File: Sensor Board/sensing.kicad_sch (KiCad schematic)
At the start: 12 parts, among them J4 CAN Bus Connector, U2 INA180, U5 INA180

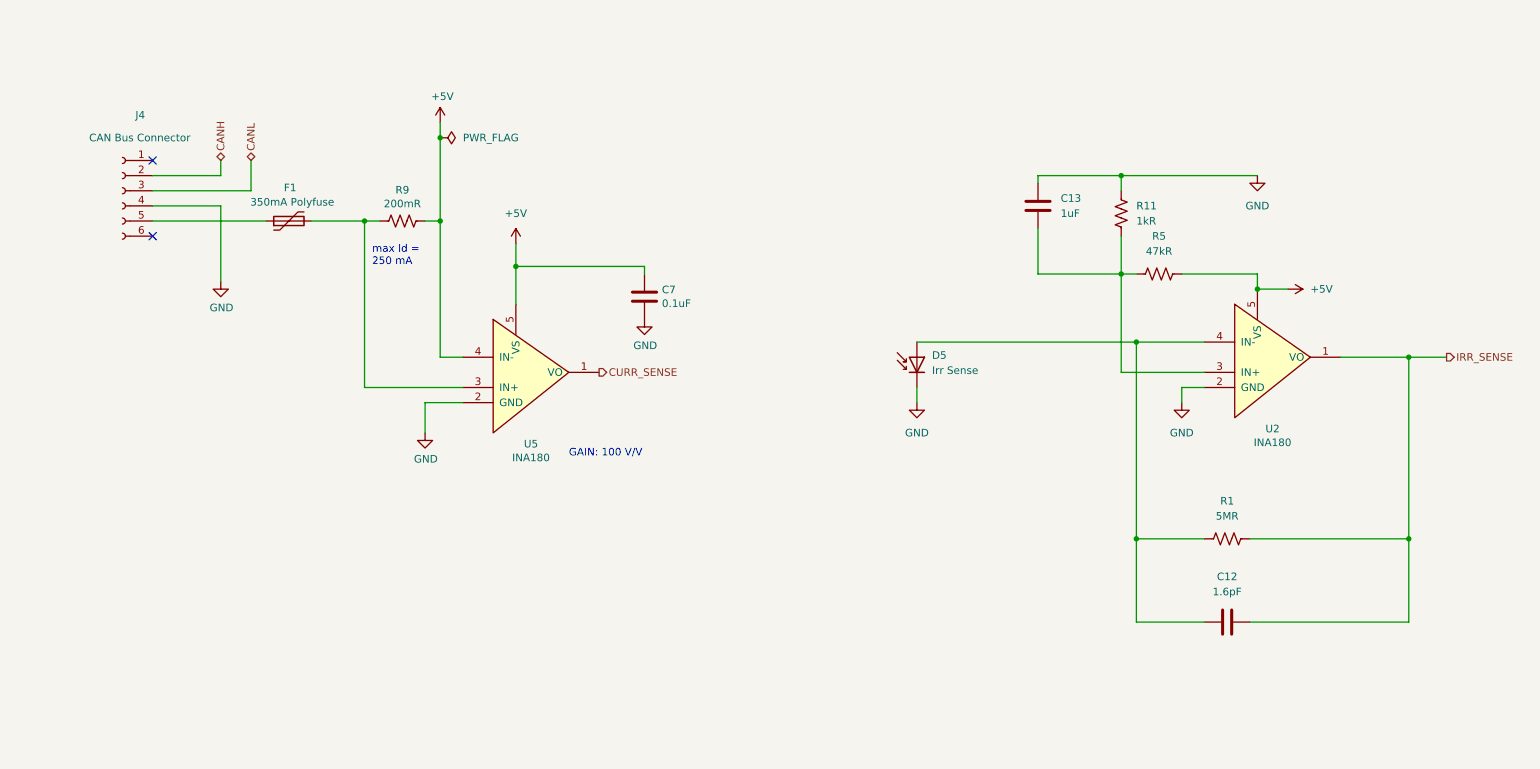
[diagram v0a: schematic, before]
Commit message: Switch op amp
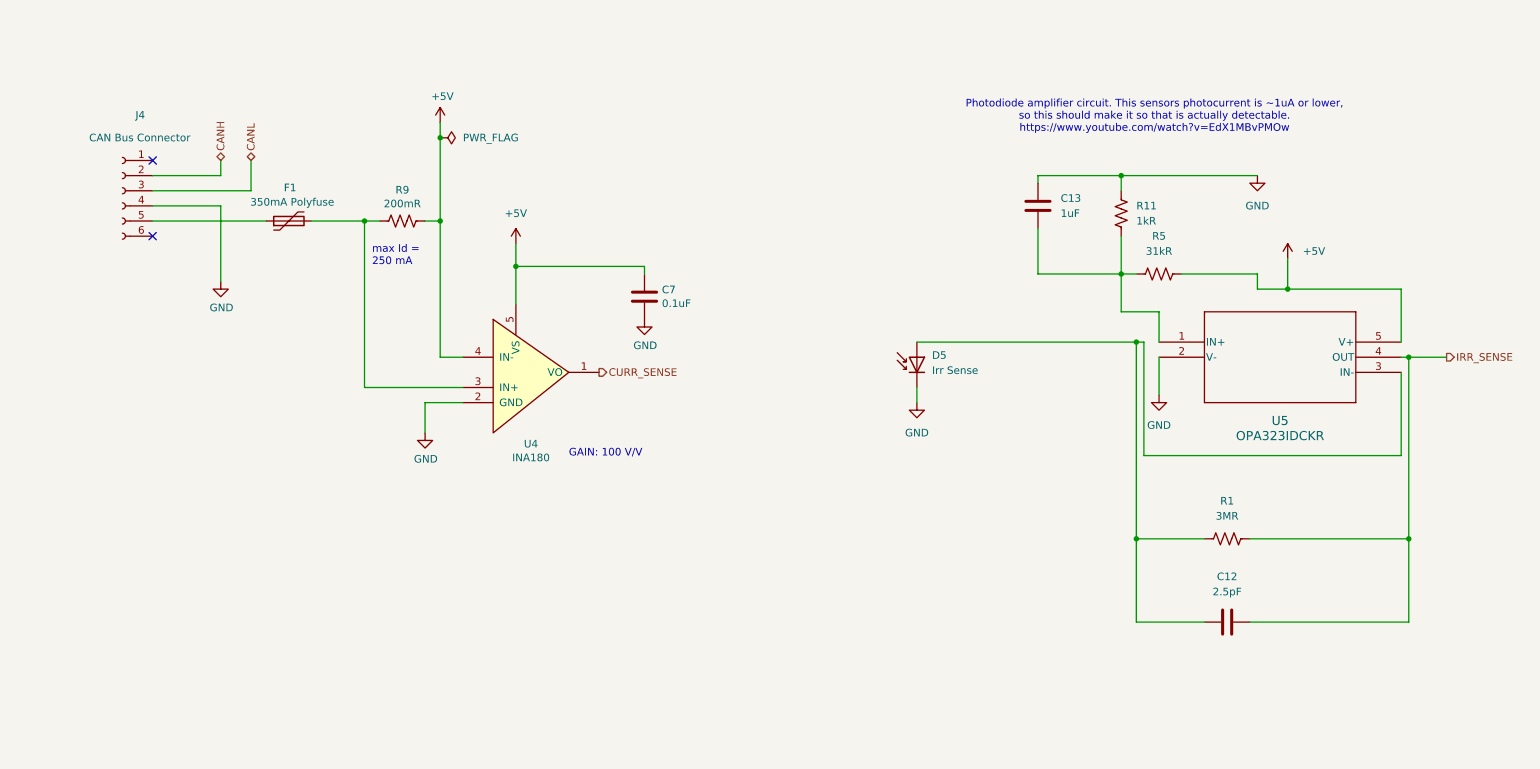
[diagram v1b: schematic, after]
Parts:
- removed U2: INA180, Package_TO_SOT_SMD:SOT-23-5_HandSoldering, symbol canhw:INA180
- added U5: OPA323IDCKR, SC70-5_DCK_TEX, symbol opa323:OPA323IDCKR
- C12: value 1.6pF -> 2.5pF
- R1: value 5MR -> 3MR
- R5: value 47kR -> 31kR
- renumbered U5 to U4
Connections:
- net +5V: now also U5.5 (V+)
- net GND: now also U5.2 (V-)
- net IRR_SENSE: now also U5.4 (OUT)
- net at C13.2, R11.1, R5.1: now also U5.1 (IN+)
- net at C12.2, D5.2 (A), R1.1: now also U5.3 (IN-)
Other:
- note added: "Photodiode amplifier circuit. This sensors photocurrent is ~1uA or lower, so this should make it so that is actually detectable. https://www.youtube.com/watch?v=EdX1MBvPMOw"

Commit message: Cooked another layout-Pranav
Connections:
- net +5V: no longer R5.2
- new net +3.3V: R5.2
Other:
- moved on the sheet: C13, D5, R11, R5

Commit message: updated optics front end
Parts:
- removed C12: 2.5pF, Capacitor_SMD:C_0805_2012Metric_Pad1.18x1.45mm_HandSolder, symbol Device:C
- removed C13: 1uF, Capacitor_SMD:C_0805_2012Metric_Pad1.18x1.45mm_HandSolder, symbol Device:C
- removed C7: 0.1uF, Capacitor_SMD:C_0805_2012Metric_Pad1.18x1.45mm_HandSolder, symbol Device:C
- removed D5: Irr Sense, Canhw:P16612-011CA, symbol Device:D_Photo
- removed F1: 350mA Polyfuse, Fuse:Fuse_1206_3216Metric_Pad1.42x1.75mm_HandSolder, symbol Device:Polyfuse
- removed J4: CAN Bus Connector, Canhw:connector_Harwin_G125–MG10605M4P, symbol Connector:Conn_01x06_Socket
- removed U4: INA180, Package_TO_SOT_SMD:SOT-23-5_HandSoldering, symbol canhw:INA180
- removed U5: OPA323IDCKR, SC70-5_DCK_TEX, symbol opa323:OPA323IDCKR
- added C12: 1uF, symbol Device:C_Small
- added C13, C14, C15, C16, C17: 0.1uF, symbol Device:C_Small
- added C18, C19: 2.2uF, symbol Device:C_Small
- added C7: 4.7pF, symbol Device:C_Small
- added D1: P16612-011CA, symbol Device:D_Filled
- added R13: 10R, symbol Device:R_US
- added U4: OPA323, Package_TO_SOT_SMD:SOT-23-5, symbol Amplifier_Operational:OPA196xDBV
- added U5: MCP3561-E/ST, TSSOP20_ST_MCH, symbol PayloadSensorSymbols:MCP3561-E_ST
- added U7: MCP1501-25xSN, Package_SO:SOIC-8_3.9x4.9mm_P1.27mm, symbol Reference_Voltage:MCP1501-25xSN
- R1: value 3MR -> 3.2M; footprint Resistor_SMD:R_0805_2012Metric_Pad1.20x1.40mm_HandSolder -> (none)
- R11: value 1kR -> 10R; footprint Resistor_SMD:R_0805_2012Metric_Pad1.20x1.40mm_HandSolder -> (none)
- R5: value 31kR -> 9.31k; footprint Resistor_SMD:R_0805_2012Metric_Pad1.20x1.40mm_HandSolder -> (none)
- R9: value 200mR -> 287R; footprint Resistor_SMD:R_0805_2012Metric_Pad1.20x1.40mm_HandSolder -> (none); DigiKey WSLB-.20CT-ND -> (none)
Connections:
- net +3.3V is gone; now on an unnamed net: R5.2
- net GND: now also C15.2, C16.2, U5.11 (NC), U5.19 (DGND); no longer R11.2
- net +3V3A: now reaches R11.1, R5.1
- net +3V3A: now also C17.1, C18.1, R13.1, U4.5 (V+), U7.1 (VDD), U7.3 (~{SHDN})
- net at R1.1: now also C7.1, D1.2 (A), U4.4 (-)
- net at R9.2: now also C12.2, U4.3 (+)
- net +5V renamed AGND
- net AGND: now also C12.1, C13.1, C14.1, C17.2, C18.2, C19.2, D1.1 (K), U4.2 (V-), U5.10 (NC), U5.2 (AGND), U5.3 (REFIN-), U5.6 (CH1), U5.9 (NC), U7.2 (GND), U7.4 (GND), U7.5 (GND), U7.6 (GND)
- net IRR_SENSE: no longer names the net of R1.2
- net IRR_SENSE: now also C7.2, U4.1, U5.5 (CH0)
- new net: C13.2, C14.2, R11.2, U5.1 (AVDD)
- new net: C15.1, C16.1, R13.2, U5.20 (DVDD)
- new net: C19.1, U5.4 (REFIN+), U5.8 (NC), U7.7 (OUT), U7.8 (FB)
- new net CS: U5.13 (*CS)
- new net IRQ/MDAT: U5.17 (*IRQ/MDAT)
- new net MCLKIN: U5.18 (MCLKIN)
- new net MISO: U5.16 (SDO)
- new net MOSI: U5.15 (SDI)
- new net SCLK: U5.14 (SCK)
- no-connect marks 2 -> 0
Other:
- note added: "Design Goals: I_{min} = 0A I_{max} = 1uA Assuming Output Swing of 50mV V_{oMin} = 50mV V_{oMax} = 3.25V f_{p} = 10kHz V_{cc} = 3.3V V_{ee} = 0V V_{ref} = 0.1V Design Values: C_{J} = 0.5pF C_{d} = 2pF C_{cm} = 1pF Design Notes: Required GBW = 18.5kHz; OPA323 GBW = 20MHz ${cf09fdd2-d5e0-47ab-9654-138cc2b941d7:REFERENCE} and ${8929b5c6-444c-41f2-87df-a3d3b9d879dc:REFERENCE} 1% tolerance"
- note added: "TIA designed referencing TI Reference Design: https://www.ti.com/lit/an/sboa220b/sboa220b.pdf?ts=1747595142490"
- note added: "Voltage Reference w/ Buffer"
- note removed: "GAIN: 100 V/V"
- note removed: "Photodiode amplifier circuit. This sensors photocurrent is ~1uA or lower, so this should make it so that is actually detectable. https://www.youtube.com/watch?v=EdX1MBvPMOw"
- note removed: "max Id = 250 mA"

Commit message: added footprints. Custom footprint for photodiode
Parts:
- C12, C13, C14, C15, C16, C17, C18, C19, C7: footprint (none) -> Capacitor_SMD:C_0805_2012Metric_Pad1.18x1.45mm_HandSolder
- D1: footprint (none) -> SensorBoardFootprints:P16612-011CA
- R1, R11, R13, R5, R9: footprint (none) -> Resistor_SMD:R_0805_2012Metric_Pad1.20x1.40mm_HandSolder
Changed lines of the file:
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@@
 			)
 		)
-		(property "Footprint" ""
+		(property "Footprint" "Resistor_SMD:R_0805_2012Metric_Pad1.20x1.40mm_HandSolder"
 			(at 159.766 33.274 90)
 			(effects
@@
 			)
 		)
-		(property "Footprint" ""
+		(property "Footprint" "Resistor_SMD:R_0805_2012Metric_Pad1.20x1.40mm_HandSolder"
 			(at 215.646 33.274 90)
 			(effects
@@
 			)
 		)
-		(property "Footprint" ""
+		(property "Footprint" "Capacitor_SMD:C_0805_2012Metric_Pad1.18x1.45mm_HandSolder"
 			(at 135.89 134.62 0)
 			(effects
@@
 			)
 		)
-		(property "Footprint" ""
+		(property "Footprint" "Capacitor_SMD:C_0805_2012Metric_Pad1.18x1.45mm_HandSolder"
 			(at 86.36 64.77 0)
 			(effects
@@
 			)
 		)
-		(property "Footprint" ""
+		(property "Footprint" "Capacitor_SMD:C_0805_2012Metric_Pad1.18x1.45mm_HandSolder"
 			(at 115.57 109.22 0)
 			(effects
@@
 			)
 		)
-		(property "Footprint" ""
+		(property "Footprint" "Capacitor_SMD:C_0805_2012Metric_Pad1.18x1.45mm_HandSolder"
 			(at 167.64 43.18 0)
 			(effects
@@
 			)
 		)
-		(property "Footprint" ""
+		(property "Footprint" "Capacitor_SMD:C_0805_2012Metric_Pad1.18x1.45mm_HandSolder"
 			(at 167.64 52.07 0)
 			(effects
@@
 			)
 		)
-		(property "Footprint" ""
+		(property "Footprint" "Capacitor_SMD:C_0805_2012Metric_Pad1.18x1.45mm_HandSolder"
 			(at 207.01 50.8 0)
 			(effects
@@
 			)
 		)
-		(property "Footprint" ""
+		(property "Footprint" "Resistor_SMD:R_0805_2012Metric_Pad1.20x1.40mm_HandSolder"
 			(at 86.614 73.914 90)
 			(effects
@@
 			)
 		)
-		(property "Footprint" ""
+		(property "Footprint" "Capacitor_SMD:C_0805_2012Metric_Pad1.18x1.45mm_HandSolder"
 			(at 207.01 41.91 0)
 			(effects
@@
 			)
 		)
-		(property "Footprint" ""
+		(property "Footprint" "SensorBoardFootprints:P16612-011CA"
 			(at 87.63 88.9 0)
 			(effects
@@
 			)
 		)
-		(property "Footprint" ""
+		(property "Footprint" "Resistor_SMD:R_0805_2012Metric_Pad1.20x1.40mm_HandSolder"
 			(at 101.346 68.326 90)
 			(effects
@@
 			)
 		)
-		(property "Footprint" ""
+		(property "Footprint" "Resistor_SMD:R_0805_2012Metric_Pad1.20x1.40mm_HandSolder"
 			(at 115.824 98.044 90)
 			(effects
@@
 			)
 		)
-		(property "Footprint" ""
+		(property "Footprint" "Capacitor_SMD:C_0805_2012Metric_Pad1.18x1.45mm_HandSolder"
 			(at 100.33 121.92 0)
 			(effects
@@
 			)
 		)
-		(property "Footprint" ""
+		(property "Footprint" "Capacitor_SMD:C_0805_2012Metric_Pad1.18x1.45mm_HandSolder"
 			(at 90.17 121.92 0)
 			(effects

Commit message: fixed footprints not loading
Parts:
- U5: footprint TSSOP20_ST_MCH -> (none)
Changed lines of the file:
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@@
 			)
 		)
-		(property "Footprint" "TSSOP20_ST_MCH"
+		(property "Footprint" ""
 			(at 158.75 67.31 0)
 			(effects

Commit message: did layout
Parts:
- added C23: 0.1uF, Capacitor_SMD:C_0805_2012Metric_Pad1.18x1.45mm_HandSolder, symbol Device:C_Small
- U5: footprint (none) -> Package_SO:TSSOP-20_4.4x6.5mm_P0.65mm
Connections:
- net +3V3A: now also C23.1; no longer R13.1
- net AGND: now also C23.2
- new net +3V3D: R13.1
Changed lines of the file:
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@@
+	(wire
+		(pts
+			(xy 120.65 68.58) (xy 120.65 67.31)
+		)
+		(stroke
+			(width 0)
+			(type default)
+		)
+	)
+	(wire
+		(pts
+			(xy 110.49 67.31) (xy 113.03 67.31)
+		)
+		(stroke
+			(width 0)
+			(type default)
+		)
+	)
 	(wire
 		(pts
@@
 		(pts
 			(xy 100.33 99.06) (xy 100.33 80.01)
+		)
+		(stroke
+			(width 0)
+			(type default)
+		)
+	)
+	(wire
+		(pts
+			(xy 120.65 67.31) (xy 118.11 67.31)
 		)
 		(stroke
@@
 	)
 	(symbol
+		(lib_id "power:GNDA")
+		(at 120.65 68.58 0)
+		(unit 1)
+		(exclude_from_sim no)
+		(in_bom yes)
+		(on_board yes)
+		(dnp no)
+		(fields_autoplaced yes)
+		(property "Reference" "#PWR5"
+			(at 120.65 74.93 0)
+			(effects
+				(font
+					(size 1.27 1.27)
+				)
+				(hide yes)
+			)
+		)
+		(property "Value" "AGND"
+			(at 120.65 73.66 0)
+			(effects
+				(font
+					(size 1.27 1.27)
+				)
+			)
+		)
+		(property "Footprint" ""
+			(at 120.65 68.58 0)
+			(effects
+				(font
+					(size 1.27 1.27)
+				)
+				(hide yes)
+			)
+		)
+		(property "Datasheet" ""
+			(at 120.65 68.58 0)
+			(effects
+				(font
+					(size 1.27 1.27)
+				)
+				(hide yes)
+			)
+		)
+		(property "Description" "Power symbol creates a global label with name \"GNDA\" , analog ground"
+			(at 120.65 68.58 0)
+			(effects
+				(font
+					(size 1.27 1.27)
+				)
+				(hide yes)
+			)
+		)
+		(pin "1"
+		)
+		(instances
+			(project "Sensor Board"
+				(path "/82a9869f-36b9-4173-b7be-dd71d5b66335/cba3e165-ed91-47ad-a83d-245f40c489c2"
+					(reference "#PWR5")
+					(unit 1)
+				)
+			)
+		)
+	)
+	(symbol
 		(lib_id "Device:C_Small")
 		(at 115.57 109.22 90)
@@
 			)
 		)
-		(property "Value" "+3V3A"
+		(property "Value" "+3V3D"
 			(at 211.328 20.828 0)
 			(effects
@@
 				(path "/82a9869f-36b9-4173-b7be-dd71d5b66335/cba3e165-ed91-47ad-a83d-245f40c489c2"
 					(reference "#PWR37")
+					(unit 1)
+				)
+			)
+		)
+	)
+	(symbol
+		(lib_id "Device:C_Small")
+		(at 115.57 67.31 90)
+		(unit 1)
+		(exclude_from_sim no)
+		(in_bom yes)
+		(on_board yes)
+		(dnp no)
+		(fields_autoplaced yes)
+		(property "Reference" "C23"
+			(at 115.5763 60.96 90)
+			(effects
+				(font
+					(size 1.27 1.27)
+				)
+			)
+		)
+		(property "Value" "0.1uF"
+			(at 115.5763 63.5 90)
+			(effects
+				(font
+					(size 1.27 1.27)
+				)
+			)
+		)
+		(property "Footprint" "Capacitor_SMD:C_0805_2012Metric_Pad1.18x1.45mm_HandSolder"
+			(at 115.57 67.31 0)
+			(effects
+				(font
+					(size 1.27 1.27)
+				)
+				(hide yes)
+			)
+		)
+		(property "Datasheet" "~"
+			(at 115.57 67.31 0)
+			(effects
+				(font
+					(size 1.27 1.27)
+				)
+				(hide yes)
+			)
+		)
+		(property "Description" "Unpolarized capacitor, small symbol"
+			(at 115.57 67.31 0)
+			(effects
+				(font
+					(size 1.27 1.27)
+				)
+				(hide yes)
+			)
+		)
+		(pin "2"
+		)
+		(pin "1"
+		)
+		(instances
+			(project "Sensor Board"
+				(path "/82a9869f-36b9-4173-b7be-dd71d5b66335/cba3e165-ed91-47ad-a83d-245f40c489c2"
+					(reference "C23")
 					(unit 1)
 				)
@@
 			)
 		)
-		(property "Footprint" ""
+		(property "Footprint" "Package_SO:TSSOP-20_4.4x6.5mm_P0.65mm"
 			(at 158.75 67.31 0)
 			(effects
@@
 		(on_board yes)
 		(dnp no)
-		(fields_autoplaced yes)
 		(property "Reference" "U4"
-			(at 123.19 71.1514 0)
+			(at 117.094 81.28 0)
 			(effects
 				(font
@@
 		)
 		(property "Value" "OPA323"
-			(at 123.19 73.6914 0)
-			(effects
-				(font
+			(at 117.094 83.82 0)
+			(effects
+				(font

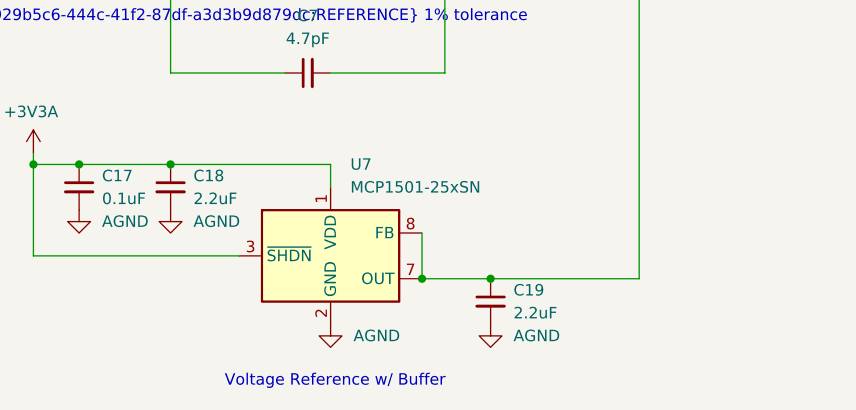
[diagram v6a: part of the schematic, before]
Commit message: implemented Joe's comments
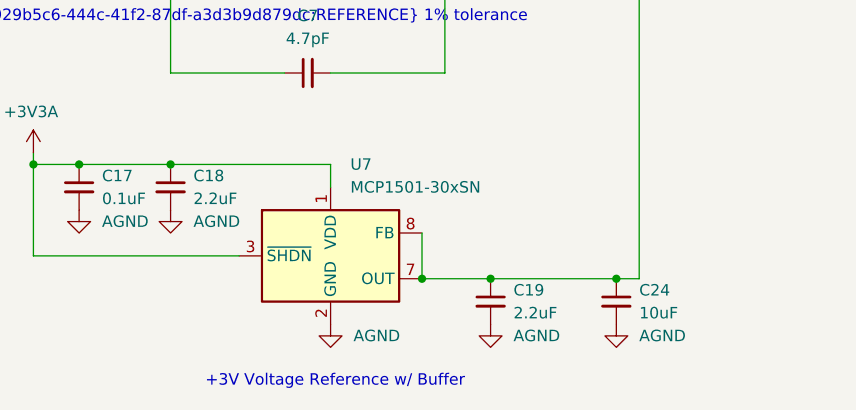
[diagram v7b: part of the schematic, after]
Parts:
- added C24: 10uF, Capacitor_SMD:C_0805_2012Metric_Pad1.18x1.45mm_HandSolder, symbol Device:C_Small
- U7: value MCP1501-25xSN -> MCP1501-30xSN
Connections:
- net AGND: now also C24.2
- net at C19.1, U5.4 (REFIN+), U5.8 (NC)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: now also C24.1
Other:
- note added: "+3V Voltage Reference w/ Buffer"
- note removed: "Voltage Reference w/ Buffer"
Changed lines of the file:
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@@
+	)
+	(junction
+		(at 149.86 132.08)
+		(diameter 0)
+		(color 0 0 0 0)
 	)
 	(junction
@@
 	(wire
 		(pts
+			(xy 149.86 132.08) (xy 152.4 132.08)
+		)
+		(stroke
+			(width 0)
+			(type default)
+		)
+	)
+	(wire
+		(pts
 			(xy 130.81 77.47) (xy 130.81 99.06)
 		)
@@
 	(wire
 		(pts
-			(xy 135.89 132.08) (xy 152.4 132.08)
+			(xy 135.89 132.08) (xy 149.86 132.08)
 		)
 		(stroke
@@
 		)
 	)
-	(text "Voltage Reference w/ Buffer"
+	(text "+3V Voltage Reference w/ Buffer"
 		(exclude_from_sim no)
 		(at 118.618 143.51 0)
@@
 	)
 	(symbol
+		(lib_id "power:GND")
+		(at 149.86 137.16 0)
+		(unit 1)
+		(exclude_from_sim no)
+		(in_bom yes)
+		(on_board yes)
+		(dnp no)
+		(fields_autoplaced yes)
+		(property "Reference" "#PWR51"
+			(at 149.86 143.51 0)
+			(effects
+				(font
+					(size 1.27 1.27)
+				)
+				(hide yes)
+			)
+		)
+		(property "Value" "AGND"
+			(at 152.4 138.4299 0)
+			(effects
+				(font
+					(size 1.27 1.27)
+				)
+				(justify left)
+			)
+		)
+		(property "Footprint" ""
+			(at 149.86 137.16 0)
+			(effects
+				(font
+					(size 1.27 1.27)
+				)
+				(hide yes)
+			)
+		)
+		(property "Datasheet" ""
+			(at 149.86 137.16 0)
+			(effects
+				(font
+					(size 1.27 1.27)
+				)
+				(hide yes)
+			)
+		)
+		(property "Description" "Power symbol creates a global label with name \"GND\" , ground"
+			(at 149.86 137.16 0)
+			(effects
+				(font
+					(size 1.27 1.27)
+				)
+				(hide yes)
+			)
+		)
+		(pin "1"
+		)
+		(instances
+			(project "Sensor Board"
+				(path "/82a9869f-36b9-4173-b7be-dd71d5b66335/cba3e165-ed91-47ad-a83d-245f40c489c2"
+					(reference "#PWR51")
+					(unit 1)
+				)
+			)
+		)
+	)
+	(symbol
 		(lib_id "power:+3V3")
 		(at 214.63 25.4 0)
@@
 			)
 		)
-		(property "Value" "MCP1501-25xSN"
+		(property "Value" "MCP1501-30xSN"
 			(at 120.3041 121.92 0)
 			(effects
@@
 			)
 		)
-		(property "Datasheet" "https://www.digikey.ca/en/products/detail/microchip-technology/MCP1501-25E-SN/5844596"
+		(property "Datasheet" "https://www.digikey.ca/en/products/detail/microchip-technology/MCP1501-30E-SN/5844597?s=N4IgTCBcDaILIGEAKBGArABhQWgMwZAF0BfIA"
 			(at 123.19 129.54 0)
 			(effects
@@
 					(unit 1)
 				)
+			)
+		)
+	)
+	(symbol
+		(lib_id "Device:C_Small")
+		(at 149.86 134.62 0)
+		(unit 1)
+		(exclude_from_sim no)
+		(in_bom yes)
+		(on_board yes)
+		(dnp no)
+		(fields_autoplaced yes)
+		(property "Reference" "C24"
+			(at 152.4 133.3562 0)
+			(effects
+				(font
+					(size 1.27 1.27)
+				)
+				(justify left)
+			)
+		)
+		(property "Value" "10uF"
+			(at 152.4 135.8962 0)
+			(effects
+				(font
+					(size 1.27 1.27)
+				)
+				(justify left)
+			)
+		)
+		(property "Footprint" "Capacitor_SMD:C_0805_2012Metric_Pad1.18x1.45mm_HandSolder"
+			(at 149.86 134.62 0)
+			(effects
+				(font
+					(size 1.27 1.27)
+				)
+				(hide yes)
+			)
+		)
+		(property "Datasheet" "~"
+			(at 149.86 134.62 0)
+			(effects
+				(font
+					(size 1.27 1.27)
+				)
+				(hide yes)
+			)
+		)
+		(property "Description" "Unpolarized capacitor, small symbol"
+			(at 149.86 134.62 0)
+			(effects
+				(font
+					(size 1.27 1.27)
+				)
+				(hide yes)
+			)
+		)
+		(pin "2"
+		)
+		(pin "1"
+		)
+		(instances
+			(project "Sensor Board"
+				(path "/82a9869f-36b9-4173-b7be-dd71d5b66335/cba3e165-ed91-47ad-a83d-245f40c489c2"
+					(reference "C24")
+					(unit 1)
+				)
